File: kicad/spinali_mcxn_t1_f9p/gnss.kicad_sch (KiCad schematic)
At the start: 63 parts, among them J3 UART, SW1 SW_SPST, SW2 SW_SPST, U2 PCMF1USB3SZ, U3 AP2112K-3.3, U4 AP2112K-3.3, U5 NEO-F9P-15B

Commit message: Adjust pages and visibilty of part numbers
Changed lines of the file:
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@@
 	(text "Place next to U5"
 		(exclude_from_sim no)
-		(at 188.214 48.514 0)
+		(at 183.642 46.228 0)
 		(effects
 			(font
@@
 					(size 1.27 1.27)
 				)
+				(hide yes)
 			)
 		)
@@
 					(size 1.27 1.27)
 				)
+				(hide yes)
 			)
 		)
@@
 					(size 1.27 1.27)
 				)
+				(hide yes)
 			)
 		)
@@
 					(size 1.27 1.27)
 				)
+				(hide yes)
 			)
 		)
@@
 					(size 1.27 1.27)
 				)
+				(hide yes)
 			)
 		)
@@
 					(size 1.27 1.27)
 				)
+				(hide yes)
 			)
 		)
@@
 					(size 1.27 1.27)
 				)
+				(hide yes)
 			)
 		)
@@
 					(size 1.27 1.27)
 				)
+				(hide yes)
 			)
 		)
@@
 					(size 1.27 1.27)
 				)
+				(hide yes)
 			)
 		)
@@
 					(size 1.27 1.27)
 				)
+				(hide yes)
 			)
 		)
@@
 					(size 1.27 1.27)
 				)
+				(hide yes)
 			)
 		)
@@
 					(size 1.27 1.27)
 				)
+				(hide yes)
 			)
 		)
@@
 		(fields_autoplaced yes)
 		(property "Reference" "C18"
-			(at 182.88 53.3399 0)
+			(at 182.88 50.7999 0)
 			(effects
 				(font
@@
 		)
 		(property "Value" "100nF 10V"
-			(at 182.88 55.8799 0)
+			(at 182.88 53.3399 0)
 			(effects
 				(font
@@
 		)
 		(property "DigiKey" "399-C0603C104K8RACTUCT-ND"
-			(at 179.07 54.61 0)
+			(at 182.88 55.8799 0)
 			(effects
 				(font
 					(size 1.27 1.27)
 				)
+				(justify left)
+				(hide yes)
 			)
 		)
@@
 					(size 1.27 1.27)
 				)
+				(hide yes)
 			)
 		)
 		(property "MFPN" "C0603C104K8RACTU"
-			(at 179.07 54.61 0)
+			(at 182.88 58.4199 0)
 			(effects
 				(font
 					(size 1.27 1.27)
 				)
+				(justify left)
+				(hide yes)
 			)
 		)
@@
 					(size 1.27 1.27)
 				)
+				(hide yes)
 			)
 		)
@@
 					(size 1.27 1.27)
 				)
+				(hide yes)
 			)
 		)
@@
 					(size 1.27 1.27)
 				)
+				(hide yes)
 			)
 		)
@@
 					(size 1.27 1.27)
 				)
+				(hide yes)
 			)
 		)
@@
 					(size 1.27 1.27)
 				)
+				(hide yes)
 			)
 		)
@@
 					(size 1.27 1.27)
 				)
+				(hide yes)
 			)
 		)
@@
 					(size 1.27 1.27)
 				)
+				(hide yes)
 			)
 		)
@@
 					(size 1.27 1.27)
 				)
+				(hide yes)
 			)
 		)
@@
 					(size 1.27 1.27)
 				)
+				(hide yes)
 			)
 		)
@@
 					(size 1.27 1.27)
 				)
+				(hide yes)
 			)
 		)
@@
 					(size 1.27 1.27)
 				)
+				(hide yes)
 			)
 		)
@@
 		(fields_autoplaced yes)
 		(property "Reference" "C14"
-			(at 143.51 38.0999 0)
+			(at 143.51 36.8299 0)
 			(effects
 				(font
@@
 		)
 		(property "Value" "1uF 10V"
-			(at 143.51 40.6399 0)
+			(at 143.51 39.3699 0)
 			(effects
 				(font
@@
 					(size 1.27 1.27)
 				)
+				(hide yes)
 			)
 		)
 		(property "MF" "Murata Electronics"
-			(at 139.7 39.37 0)
+			(at 143.51 41.9099 0)
 			(effects
 				(font
 					(size 1.27 1.27)
 				)
+				(justify left)
+				(hide yes)
 			)
 		)
@@
 					(size 1.27 1.27)
 				)
+				(hide yes)
 			)
 		)
@@
 					(size 1.27 1.27)
 				)
+				(hide yes)
 			)
 		)
@@
 					(size 1.27 1.27)
 				)
+				(hide yes)
 			)
 		)
@@
 					(size 1.27 1.27)
 				)
+				(hide yes)
 			)
 		)
@@
 					(size 1.27 1.27)
 				)
+				(hide yes)
 			)
 		)
@@
 					(size 1.27 1.27)
 				)
+				(hide yes)
 			)
 		)
@@
 					(size 1.27 1.27)
 				)
+				(hide yes)
 			)
 		)
@@
 					(size 1.27 1.27)
 				)
+				(hide yes)
 			)
 		)
@@
 					(size 1.27 1.27)
 				)
+				(hide yes)
 			)
 		)
@@
 					(size 1.27 1.27)
 				)
+				(hide yes)
 			)
 		)
@@
 					(size 1.27 1.27)
 				)
+				(hide yes)
 			)
 		)
@@
 					(size 1.27 1.27)
 				)
+				(hide yes)
 			)
 		)
@@
 					(size 1.27 1.27)
 				)
+				(hide yes)
 			)
 		)
@@
 					(size 1.27 1.27)
 				)
+				(hide yes)
 			)
 		)
@@
 					(size 1.27 1.27)
 				)
+				(hide yes)
 			)
 		)
@@
 					(size 1.27 1.27)
 				)
+				(hide yes)
 			)
 		)
@@
 					(size 1.27 1.27)
 				)
+				(hide yes)
 			)
 		)
@@
 					(size 1.27 1.27)
 				)
+				(hide yes)
 			)
 		)
@@
 					(size 1.27 1.27)
 				)
+				(hide yes)
 			)
 		)
@@
 					(size 1.27 1.27)
 				)
+				(hide yes)
 			)
 		)
@@
 					(size 1.27 1.27)
 				)
+				(hide yes)
 			)
 		)
@@
 					(size 1.27 1.27)
 				)
+				(hide yes)
 			)
 		)
@@
 					(size 1.27 1.27)
 				)
+				(hide yes)
 			)
 		)
@@
 					(size 1.27 1.27)
 				)
+				(hide yes)
 			)
 		)
@@
 					(size 1.27 1.27)
 				)
+				(hide yes)
 			)
 		)
@@
 					(size 1.27 1.27)
 				)
+				(hide yes)
 			)
 		)
@@
 					(size 1.27 1.27)
 				)
+				(hide yes)
 			)
 		)
@@
 					(size 1.27 1.27)
 				)
+				(hide yes)
 			)
 		)

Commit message: Correct footprints for switches and battery connector
for some reason these keep getting "unlinked"
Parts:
- ANT1: footprint Connector_Coaxial:SMA_Amphenol_132134-10_Vertical -> Connector_Coaxial:U.FL_Molex_MCRF_73412-0110_Vertical
- BAT1: footprint Connector_JST:JST_SH_BM02B-SRSS-TB_1x02-1MP_P1.00mm_Vertical -> spinali-connector:JST_SH_SM02B-SRSS-TB_1x02-1MP_P1.00mm_RA
- SW1, SW2: footprint Button_Switch_SMD:SW_SPST_PTS647_Sx50 -> spinali-connector:Panasonic_EVQPUL_EVQPUC
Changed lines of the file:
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@@
 			)
 		)
-		(property "Footprint" "Connector_Coaxial:SMA_Amphenol_132134-10_Vertical"
+		(property "Footprint" "Connector_Coaxial:U.FL_Molex_MCRF_73412-0110_Vertical"
 			(at 88.9 80.01 0)
 			(effects
@@
 			)
 		)
-		(property "Footprint" "Connector_JST:JST_SH_BM02B-SRSS-TB_1x02-1MP_P1.00mm_Vertical"
+		(property "Footprint" "spinali-connector:JST_SH_SM02B-SRSS-TB_1x02-1MP_P1.00mm_RA"
 			(at 119.38 84.836 90)
 			(effects
@@
 			)
 		)
-		(property "Footprint" "Button_Switch_SMD:SW_SPST_PTS647_Sx50"
+		(property "Footprint" "spinali-connector:Panasonic_EVQPUL_EVQPUC"
 			(at 340.36 173.99 0)
 			(effects
@@
 			)
 		)
-		(property "Footprint" "Button_Switch_SMD:SW_SPST_PTS647_Sx50"
+		(property "Footprint" "spinali-connector:Panasonic_EVQPUL_EVQPUC"
 			(at 388.62 173.99 0)
 			(effects

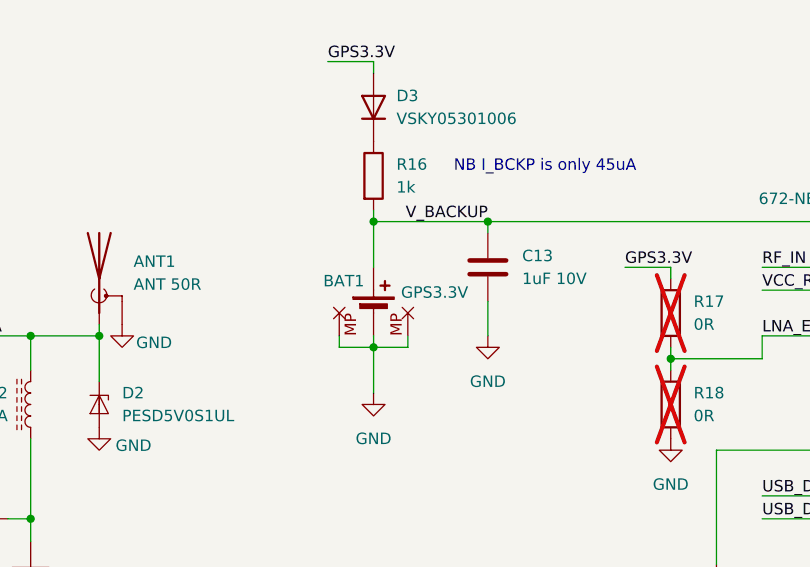
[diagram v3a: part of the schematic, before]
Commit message: Started improving layout
- Fixed library references in footprints etc.
- Fixed USB differential pair length matched
- Added GND vias to some parts where needed. (still needs more)
- Changed some routing

Signed-off-by: Youri Tils <youri.tils@nxp.com>
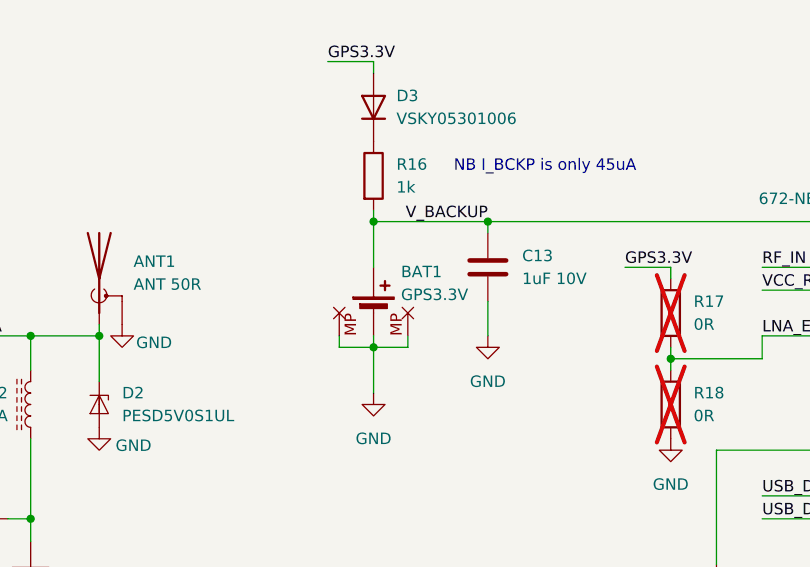
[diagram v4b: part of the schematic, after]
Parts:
- BAT1: footprint spinali-connector:JST_SH_SM02B-SRSS-TB_1x02-1MP_P1.00mm_RA -> Connectors:JST_SH_SM02B-SRSS-TB_1x02-1MP_P1.00mm_RA; MF JST -> JST Sales America Inc.; MFPN SM02B-SRSS-TB -> SM02B-SRSS-TB
- SW1, SW2: footprint spinali-connector:Panasonic_EVQPUL_EVQPUC -> Switches:Panasonic_EVQPUL_EVQPUC
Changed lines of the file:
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@@
 	)
 	(symbol
-		(lib_id "Connectors:Battery_Cell-RPI")
-		(at 119.38 86.36 0)
-		(unit 1)
-		(exclude_from_sim no)
-		(in_bom yes)
-		(on_board yes)
-		(dnp no)
-		(property "Reference" "BAT1"
-			(at 113.792 82.804 0)
-			(effects
-				(font
-					(size 1.27 1.27)
-				)
-				(justify left)
-			)
-		)
-		(property "Value" "GPS3.3V"
-			(at 122.428 84.074 0)
-			(effects
-				(font
-					(size 1.27 1.27)
-				)
-				(justify left)
-			)
-		)
-		(property "Footprint" "spinali-connector:JST_SH_SM02B-SRSS-TB_1x02-1MP_P1.00mm_RA"
-			(at 119.38 84.836 90)
-			(effects
-				(font
-					(size 1.27 1.27)
-				)
-				(hide yes)
-			)
-		)
-		(property "Datasheet" "https://www.jst.com/wp-content/uploads/2025/06/eSH.pdf"
-			(at 119.38 84.836 90)
-			(effects
-				(font
-					(size 1.27 1.27)
-				)
-				(hide yes)
-			)
-		)
-		(property "Description" "Single-cell battery"
-			(at 119.38 86.36 0)
-			(effects
-				(font
-					(size 1.27 1.27)
-				)
-				(hide yes)
-			)
-		)
-		(property "DigiKey" "455-SM02B-SRSS-TBCT-ND"
-			(at 119.38 86.36 0)
-			(effects
-				(font
-					(size 1.27 1.27)
-				)
-				(hide yes)
-			)
-		)
-		(property "MF" "JST"
-			(at 119.38 86.36 0)
-			(effects
-				(font
-					(size 1.27 1.27)
-				)
-				(hide yes)
-			)
-		)
-		(property "MFPN" "  SM02B-SRSS-TB"
-			(at 119.38 86.36 0)
-			(effects
-				(font
-					(size 1.27 1.27)
-				)
-				(hide yes)
-			)
-		)
-		(pin "2"
-		)
-		(pin "1"
-		)
-		(pin "3"
-		)
-		(pin "4"
-		)
-		(instances
-			(project "spinali_mcxn_t1_f9p"
-				(path "/04285d74-eeba-483c-9378-52bd287e15a2/984519f8-3ba1-4ad2-a1fd-5bc7d7d39895"
-					(reference "BAT1")
-					(unit 1)
-				)
-			)
-		)
-	)
-	(symbol
 		(lib_id "Device:R")
 		(at 252.73 111.76 90)
@@
 	)
 	(symbol
+		(lib_name "Battery_Cell-RPI_1")
+		(lib_id "Connectors:Battery_Cell-RPI")
+		(at 119.38 86.36 0)
+		(unit 1)
+		(exclude_from_sim no)
+		(in_bom yes)
+		(on_board yes)
+		(dnp no)
+		(property "Reference" "BAT1"
+			(at 122.428 81.788 0)
+			(effects
+				(font
+					(size 1.27 1.27)
+				)
+				(justify left)
+			)
+		)
+		(property "Value" "GPS3.3V"
+			(at 122.428 84.328 0)
+			(effects
+				(font
+					(size 1.27 1.27)
+				)
+				(justify left)
+			)
+		)
+		(property "Footprint" "Connectors:JST_SH_SM02B-SRSS-TB_1x02-1MP_P1.00mm_RA"
+			(at 119.38 108.458 0)
+			(effects
+				(font
+					(size 1.27 1.27)
+				)
+				(hide yes)
+			)
+		)
+		(property "Datasheet" "https://www.jst.com/wp-content/uploads/2025/06/eSH.pdf"
+			(at 119.38 106.172 0)
+			(effects
+				(font
+					(size 1.27 1.27)
+				)
+				(hide yes)
+			)
+		)
+		(property "Description" "Single-cell battery"
+			(at 119.38 97.79 0)
+			(effects
+				(font
+					(size 1.27 1.27)
+				)
+				(hide yes)
+			)
+		)
+		(property "MF" "JST Sales America Inc."
+			(at 119.38 102.108 0)
+			(effects
+				(font
+					(size 1.27 1.27)
+				)
+				(hide yes)
+			)
+		)
+		(property "MFPN" "SM02B-SRSS-TB"
+			(at 119.38 100.076 0)
+			(effects
+				(font
+					(size 1.27 1.27)
+				)
+				(hide yes)
+			)
+		)
+		(property "DigiKey" "455-SM02B-SRSS-TBCT-ND"
+			(at 119.38 104.14 0)
+			(effects
+				(font
+					(size 1.27 1.27)
+				)
+				(hide yes)
+			)
+		)
+		(pin "3"
+		)
+		(pin "2"
+		)
+		(pin "1"
+		)
+		(pin "4"
+		)
+		(instances
+			(project ""
+				(path "/04285d74-eeba-483c-9378-52bd287e15a2/984519f8-3ba1-4ad2-a1fd-5bc7d7d39895"
+					(reference "BAT1")
+					(unit 1)
+				)
+			)
+		)
+	)
+	(symbol
 		(lib_id "Sensors:NEO-F9P-15B")
 		(at 172.72 73.66 0)
@@
 			)
 		)
-		(property "Footprint" "spinali-connector:Panasonic_EVQPUL_EVQPUC"
+		(property "Footprint" "Switches:Panasonic_EVQPUL_EVQPUC"
 			(at 340.36 173.99 0)
 			(effects
@@
 			)
 		)
-		(property "Footprint" "spinali-connector:Panasonic_EVQPUL_EVQPUC"
+		(property "Footprint" "Switches:Panasonic_EVQPUL_EVQPUC"
 			(at 388.62 173.99 0)
 			(effects
